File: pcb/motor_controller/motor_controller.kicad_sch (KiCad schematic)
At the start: 5 parts, among them U1 STM32F446RETx, U3 DRV8323RHRGZT, U4 LDFM33PUR, U5 MA702GQ-Z, U6 MCP2542FDT-H/MNY

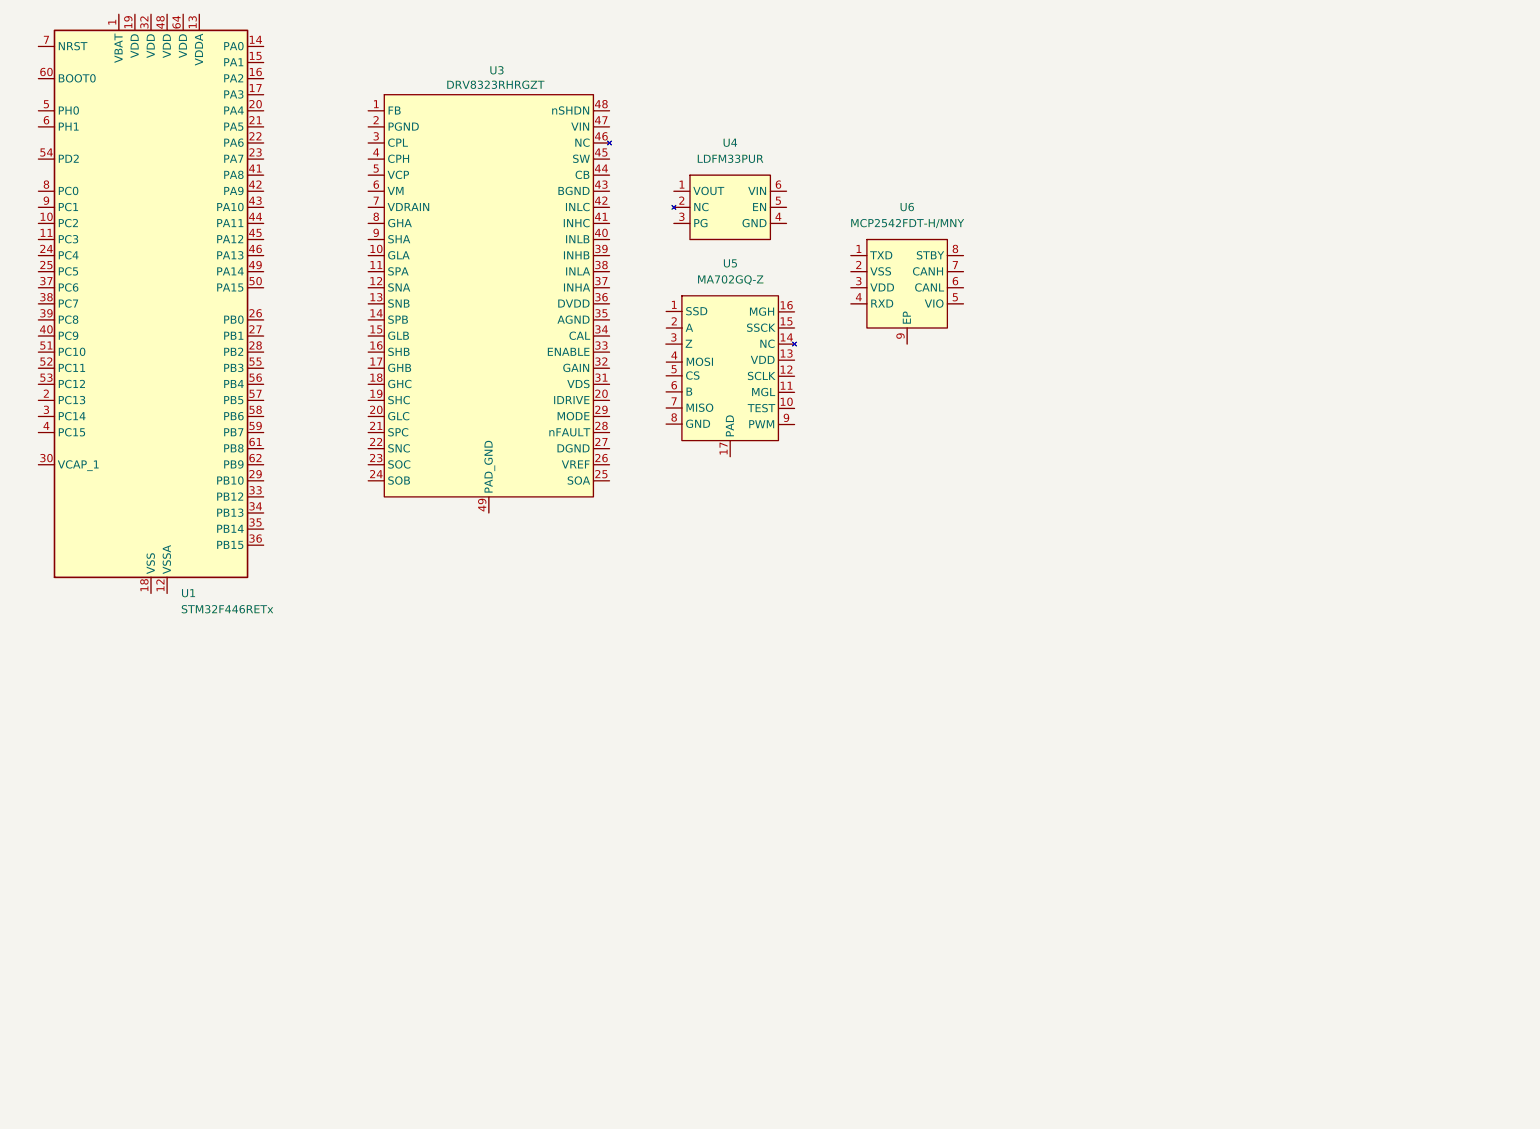
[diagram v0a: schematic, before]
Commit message: Updated symbols grouping similar pins close to eachother.
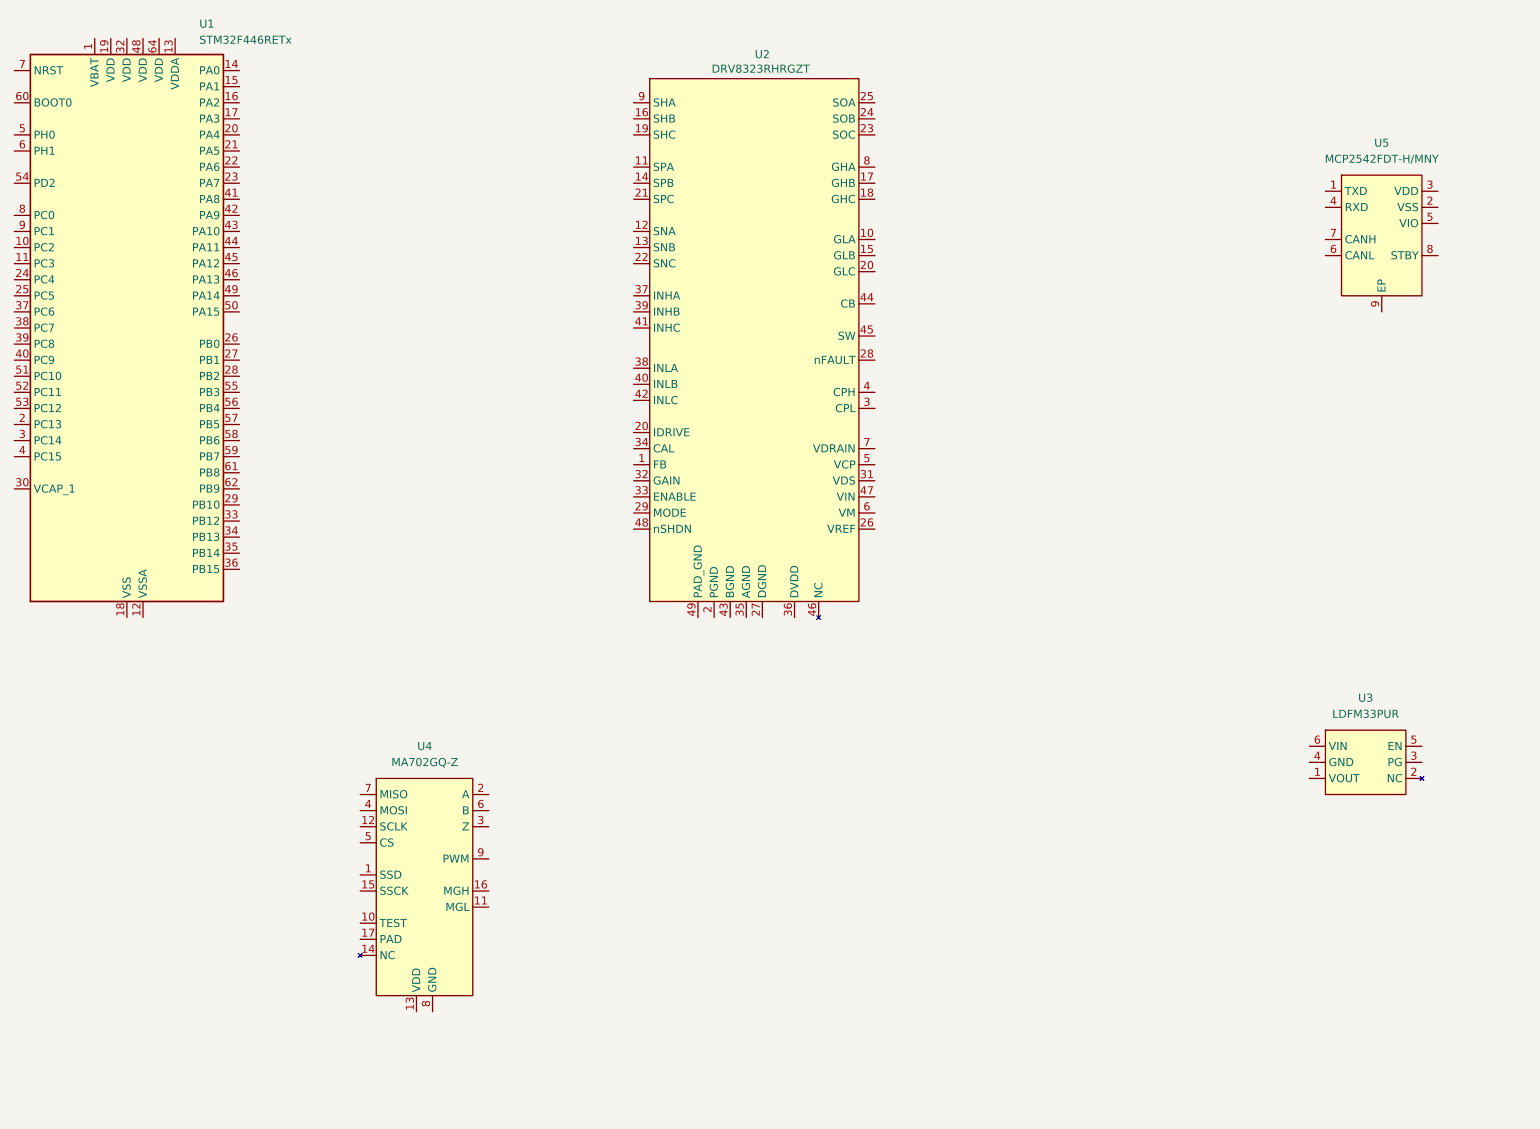
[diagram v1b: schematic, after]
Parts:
- renumbered U3 to U2, U4 to U3, U5 to U4, U6 to U5
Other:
- moved on the sheet: U1, U2, U3, U4, U5

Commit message: Latest update.
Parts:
- added C1, C2: 1uF, symbol Device:C_Small
- added C3, C4: 0.1uF, symbol Device:C_Small
- added R1: 120, symbol Device:R_Small
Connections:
- net GND: now reaches U4.10 (TEST)
- net GND: now also U3.4 (GND), U4.17 (PAD), U4.8 (GND), U5.2 (VSS), U5.9 (EP), C1.2, C2.2, C3.1, C4.1
- net MA702_MGL: now reaches U4.11 (MGL)
- net MA702_SCLK: now reaches U4.12 (SCLK)
- net MA702_VDD: now reaches U4.13 (VDD)
- net MA702_VDD: now also C1.1
- net MA702_MGH: now reaches U4.16 (MGH)
- net MA702_MOSI: now reaches U4.4 (MOSI)
- net MA702_CS: now reaches U4.5 (CS)
- net MA702_MISO: now reaches U4.7 (MISO)
- net MCP2542_TXD: now reaches U5.1 (TXD)
- net MCP2542_VDD: now reaches U5.3 (VDD)
- net MCP2542_VDD: now also C3.2
- net MCP2542_RXD: now reaches U5.4 (RXD)
- net MCP2542_VIO: now reaches U5.5 (VIO)
- net MCP2542_VIO: now also C4.2
- net MCP2542_STBY: now reaches U5.8 (STBY)
- net LDFM_VOUT: now reaches U3.1 (VOUT)
- net LDFM_PG: now reaches U3.3 (PG)
- net LDFM_EN: now reaches U3.5 (EN)
- net LDFM_VIN: now reaches U3.6 (VIN)
- net LDFM_VIN: now also C2.1
- no-connect marks 0 -> 6
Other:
- moved on the sheet: U2, U3, U4, U5
